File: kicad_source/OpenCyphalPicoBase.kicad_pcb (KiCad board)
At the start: 2 copper layers, 52 x 36 mm, 60 parts, among them CN1 RASPBERRYPI_PICO, CN11 CONN_02X03, CN12 Conn_01x03, CN2 SM04B-SRSS-TB, CN3 SM04B-SRSS-TB, CN4 GH_SM04B-GHS-TB, CN5 GH_SM04B-GHS-TB, CN6 691322310002, CN7 CONN_02X03, CN8 Conn_02x08_Odd_Even, SW1 SPST, U3 24LC64, U8 MCP2515, U9 SN65HVD232, Y1 16MHz

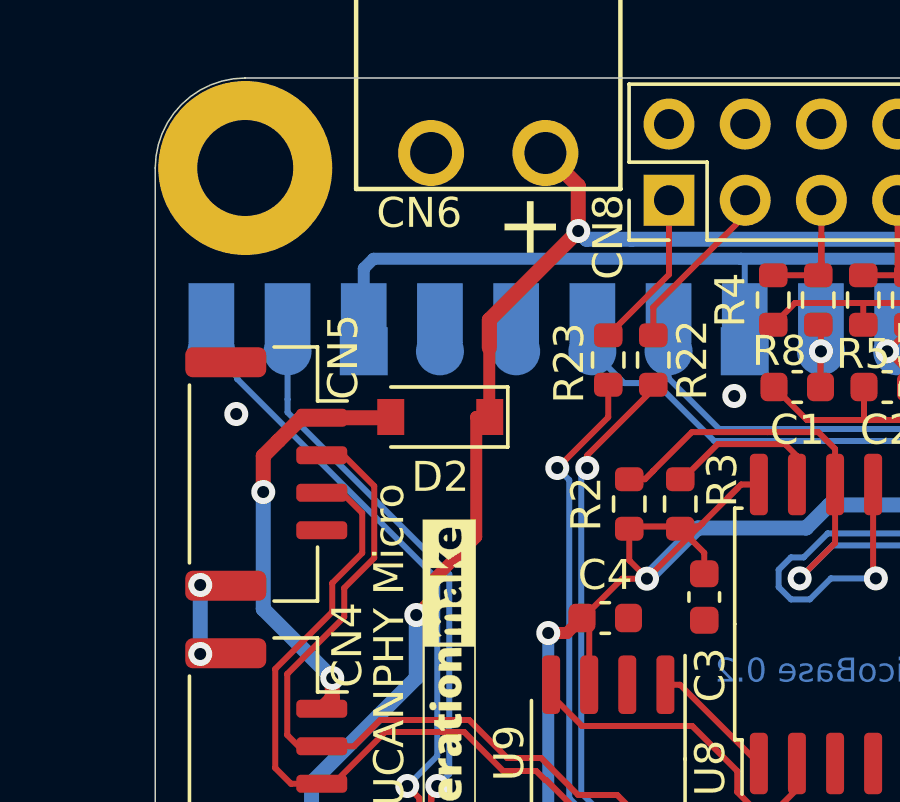
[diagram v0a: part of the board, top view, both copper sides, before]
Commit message: added poly fuse
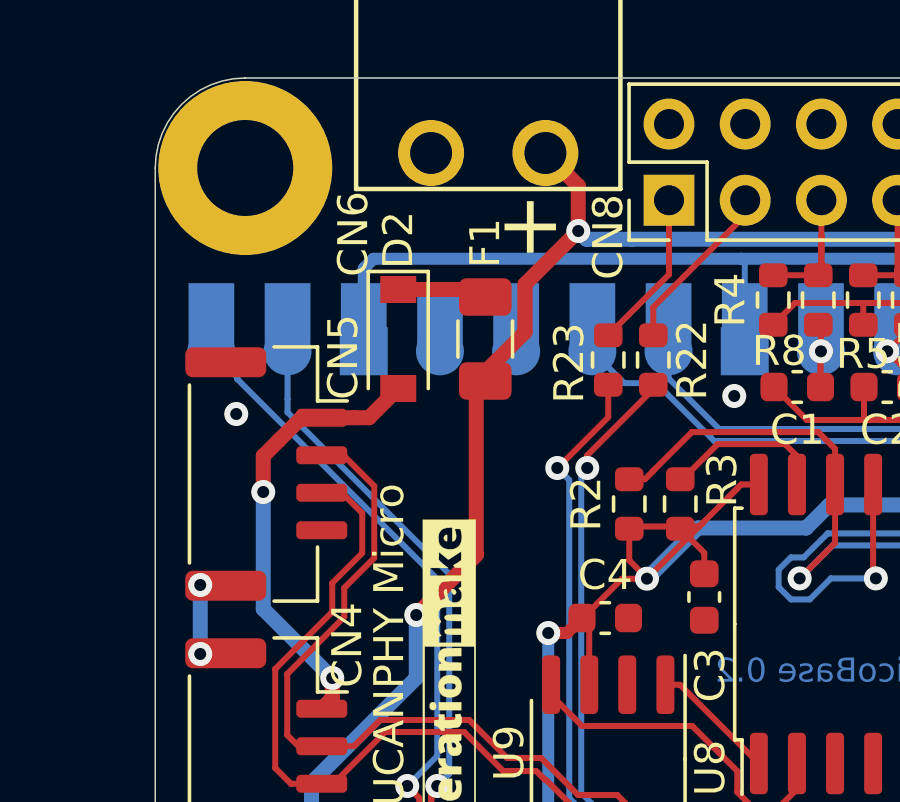
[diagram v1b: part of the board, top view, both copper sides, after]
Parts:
- added F1: nanoSMDC050F, Fuse:Fuse_1206_3216Metric, F.Cu at (75.0, 82.7)
- moved D2 2.95 mm to (72.1, 82.7), turned to -90 degrees
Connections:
- D2 pad 1: +BATT -> Net-(D2-Pad1)
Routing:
- net Net-(D2-Pad1): track 0.00 -> 4.26 mm
- net /MCP2515/CANVCC: track 14.3 -> 15.0 mm
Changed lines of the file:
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@@
   (net 65 "unconnected-(MECH4-Pad1)")
   (net 66 "unconnected-(U9-Pad5)")
+  (net 67 "Net-(D2-Pad1)")
   (footprint "MECH_mounting_holes:MHP_3.2_5.8" (layer "F.Cu")
     (at 67 77)
@@
   )
   (footprint "Diode_SMD:D_SOD-123" (layer "F.Cu")
-    (at 73.5 85.3 180)
+    (at 72.1 82.7 -90)
     (descr "SOD-123")
     (tags "SOD-123")
@@
     (property "Sheetname" "MCP2515")
     (attr smd)
-    (fp_text reference "D2" (at 0 -2 180) (layer "F.SilkS")
+    (fp_text reference "D2" (at -3.3 0 90) (layer "F.SilkS")
       (effects (font (size 1 1) (thickness 0.15)))
     )
-    (fp_text value "MBR0530T1G" (at 0 2.1 180) (layer "F.Fab")
+    (fp_text value "MBR0530T1G" (at 0 2.1 90) (layer "F.Fab")
       (effects (font (size 1 1) (thickness 0.15)))
     )
-    (fp_text user "${REFERENCE}" (at 0 -2 180) (layer "F.Fab")
+    (fp_text user "${REFERENCE}" (at 0 -2 90) (layer "F.Fab")
       (effects (font (size 1 1) (thickness 0.15)))
     )
@@
     (fp_line (start 1.4 0.9) (end -1.4 0.9) (layer "F.Fab") (width 0.1))
     (fp_line (start -1.4 0.9) (end -1.4 -0.9) (layer "F.Fab") (width 0.1))
-    (pad "1" smd rect (at -1.65 0 180) (size 0.9 1.2) (layers "F.Cu" "F.Paste" "F.Mask")
-      (net 15 "+BATT") (pinfunction "K") (pintype "passive"))
-    (pad "2" smd rect (at 1.65 0 180) (size 0.9 1.2) (layers "F.Cu" "F.Paste" "F.Mask")
+    (pad "1" smd rect (at -1.65 0 270) (size 0.9 1.2) (layers "F.Cu" "F.Paste" "F.Mask")
+      (net 67 "Net-(D2-Pad1)") (pinfunction "K") (pintype "passive"))
+    (pad "2" smd rect (at 1.65 0 270) (size 0.9 1.2) (layers "F.Cu" "F.Paste" "F.Mask")
       (net 11 "/MCP2515/CANVCC") (pinfunction "A") (pintype "passive"))
     (model "${KICAD6_3DMODEL_DIR}/Diode_SMD.3dshapes/D_SOD-123.wrl"
@@
     (property "Sheetname" "")
     (attr through_hole)
-    (fp_text reference "CN6" (at 2.3 -2) (layer "F.SilkS")
+    (fp_text reference "CN6" (at 4.5 -2.7 90) (layer "F.SilkS")
       (effects (font (size 1 1) (thickness 0.15)))
     )
@@
     )
   )
+  (footprint "Fuse:Fuse_1206_3216Metric" (layer "F.Cu")
+    (at 75 82.7 90)
+    (descr "Fuse SMD 1206 (3216 Metric), square (rectangular) end terminal, IPC_7351 nominal, (Body size source: http://www.tortai-tech.com/upload/download/2011102023233369053.pdf), generated with kicad-footprint-generator")
+    (tags "fuse")
+    (property "Sheetfile" "Datei: mcp2515.kicad_sch")
+    (property "Sheetname" "MCP2515")
+    (attr smd)
+    (fp_text reference "F1" (at 3.2 0 90) (layer "F.SilkS")
+      (effects (font (size 1 1) (thickness 0.15)))
+    )
+    (fp_text value "nanoSMDC050F" (at 0 1.82 90) (layer "F.Fab")
+      (effects (font (size 1 1) (thickness 0.15)))
+    )
+    (fp_text user "${REFERENCE}" (at 0 0 90) (layer "F.Fab")
+      (effects (font (size 0.8 0.8) (thickness 0.12)))
+    )
+    (fp_line (start -0.602064 0.91) (end 0.602064 0.91) (layer "F.SilkS") (width 0.12))
+    (fp_line (start -0.602064 -0.91) (end 0.602064 -0.91) (layer "F.SilkS") (width 0.12))
+    (fp_line (start 2.28 -1.12) (end 2.28 1.12) (layer "F.CrtYd") (width 0.05))
+    (fp_line (start -2.28 -1.12) (end 2.28 -1.12) (layer "F.CrtYd") (width 0.05))
+    (fp_line (start 2.28 1.12) (end -2.28 1.12) (layer "F.CrtYd") (width 0.05))
+    (fp_line (start -2.28 1.12) (end -2.28 -1.12) (layer "F.CrtYd") (width 0.05))
+    (fp_line (start -1.6 0.8) (end -1.6 -0.8) (layer "F.Fab") (width 0.1))
+    (fp_line (start 1.6 0.8) (end -1.6 0.8) (layer "F.Fab") (width 0.1))
+    (fp_line (start -1.6 -0.8) (end 1.6 -0.8) (layer "F.Fab") (width 0.1))
+    (fp_line (start 1.6 -0.8) (end 1.6 0.8) (layer "F.Fab") (width 0.1))
+    (pad "1" smd roundrect (at -1.4 0 90) (size 1.25 1.75) (layers "F.Cu" "F.Paste" "F.Mask") (roundrect_rratio 0.2)
+      (net 15 "+BATT") (pintype "passive"))
+    (pad "2" smd roundrect (at 1.4 0 90) (size 1.25 1.75) (layers "F.Cu" "F.Paste" "F.Mask") (roundrect_rratio 0.2)
+      (net 67 "Net-(D2-Pad1)") (pintype "passive"))
+    (model "${KICAD6_3DMODEL_DIR}/Fuse.3dshapes/Fuse_1206_3216Metric.wrl"
+      (offset (xyz 0 0 0))
+      (scale (xyz 1 1 1))
+      (rotate (xyz 0 0 0))
+    )
+  )
   (footprint "labels:generationmake_small_solder" (layer "B.Cu")
     (at 89.61905 110.93645 180)
@@
   (segment (start 69.55 85.325) (end 68.875 85.325) (width 0.5) (layer "F.Cu") (net 11))
   (segment (start 68.1 86.1) (end 67.6 86.6) (width 0.5) (layer "F.Cu") (net 11))
-  (segment (start 69.55 85.325) (end 71.84 85.325) (width 0.5) (layer "F.Cu") (net 11))
+  (segment (start 71.125 85.325) (end 72.1 84.35) (width 0.5) (layer "F.Cu") (net 11))
+  (segment (start 69.55 85.325) (end 70.625 85.325) (width 0.5) (layer "F.Cu") (net 11))
   (segment (start 68.875 85.325) (end 68.1 86.1) (width 0.5) (layer "F.Cu") (net 11))
   (segment (start 67.6 86.6) (end 67.6 87.8) (width 0.5) (layer "F.Cu") (net 11))
-  (segment (start 71.84 85.325) (end 71.865 85.3) (width 0.5) (layer "F.Cu") (net 11))
+  (segment (start 70.625 85.325) (end 71.125 85.325) (width 0.5) (layer "F.Cu") (net 11))
   (via (at 69.9 94) (size 0.8) (drill 0.4) (layers "F.Cu" "B.Cu") (net 11))
   (via (at 67.6 87.8) (size 0.8) (drill 0.4) (layers "F.Cu" "B.Cu") (net 11))
@@
   (segment (start 106.9 103.425) (end 106.7 103.225) (width 0.2) (layer "F.Cu") (net 14))
   (segment (start 78.1 79.1) (end 78.1 77.595) (width 0.5) (layer "F.Cu") (net 15))
+  (segment (start 74.7 84.1) (end 74.7 89.9) (width 0.5) (layer "F.Cu") (net 15))
   (segment (start 107.6 79.8) (end 108.2 79.2) (width 0.5) (layer "F.Cu") (net 15))
   (segment (start 105.7 85.1) (end 105.7 83.6) (width 0.5) (layer "F.Cu") (net 15))
-  (segment (start 75.135 85.3) (end 75.135 83) (width 0.4) (layer "F.Cu") (net 15))
   (segment (start 106.7 86.1) (end 105.7 85.1) (width 0.5) (layer "F.Cu") (net 15))
-  (segment (start 73.2 91.4) (end 72.7 91.9) (width 0.4) (layer "F.Cu") (net 15))
-  (segment (start 74.7 85.3) (end 75.135 85.3) (width 0.4) (layer "F.Cu") (net 15))
-  (segment (start 75.135 82.065) (end 78.1 79.1) (width 0.5) (layer "F.Cu") (net 15))
+  (segment (start 76.325 80.875) (end 76.325 82.475) (width 0.5) (layer "F.Cu") (net 15))
+  (segment (start 76.325 82.475) (end 74.7 84.1) (width 0.5) (layer "F.Cu") (net 15))
   (segment (start 78.6 103.425) (end 78.6 104.2) (width 0.2) (layer "F.Cu") (net 15))
   (segment (start 108.05 86.1) (end 106.7 86.1) (width 0.5) (layer "F.Cu") (net 15))
+  (segment (start 78.1 79.1) (end 76.325 80.875) (width 0.5) (layer "F.Cu") (net 15))
   (segment (start 105.7 83.6) (end 106.3 83) (width 0.5) (layer "F.Cu") (net 15))
   (segment (start 107.3 83) (end 107.6 82.7) (width 0.5) (layer "F.Cu") (net 15))
   (segment (start 107.6 82.7) (end 107.6 79.8) (width 0.5) (layer "F.Cu") (net 15))
-  (segment (start 74.7 89.3) (end 74.7 85.3) (width 0.4) (layer "F.Cu") (net 15))
-  (segment (start 73.2 90.8) (end 74.7 89.3) (width 0.4) (layer "F.Cu") (net 15))
-  (segment (start 75.135 83) (end 75.135 82.065) (width 0.5) (layer "F.Cu") (net 15))
   (segment (start 78.6 104.2) (end 78.9 104.5) (width 0.2) (layer "F.Cu") (net 15))
   (segment (start 78.1 77.595) (end 77.005 76.5) (width 0.5) (layer "F.Cu") (net 15))
-  (segment (start 73.2 90.8) (end 73.2 91.4) (width 0.4) (layer "F.Cu") (net 15))
   (segment (start 106.3 83) (end 107.3 83) (width 0.5) (layer "F.Cu") (net 15))
+  (segment (start 74.7 89.9) (end 72.7 91.9) (width 0.5) (layer "F.Cu") (net 15))
   (via (at 72.7 91.9) (size 0.8) (drill 0.4) (layers "F.Cu" "B.Cu") (net 15))
   (via (at 78.9 104.5) (size 0.8) (drill 0.4) (layers "F.Cu" "B.Cu") (net 15))
@@
   (segment (start 76.03 81.84) (end 76.03 83.11) (width 0.4) (layer "B.Cu") (net 60))
   (segment (start 73.49 81.84) (end 73.49 83.11) (width 0.4) (layer "B.Cu") (net 61))
+  (segment (start 73.55 81.05) (end 74.45 81.05) (width 0.5) (layer "F.Cu") (net 67))
+  (segment (start 73.55 81.05) (end 74.75 81.05) (width 0.5) (layer "F.Cu") (net 67))
+  (segment (start 73.55 81.05) (end 72.1 81.05) (width 0.5) (layer "F.Cu") (net 67))
+  (segment (start 74.45 81.05) (end 74.7 81.3) (width 0.5) (layer "F.Cu") (net 67))
+  (segment (start 74.75 81.05) (end 75 81.3) (width 0.5) (layer "F.Cu") (net 67))
   (zone (net 2) (net_name "GND") (layer "F.Cu") (hatch edge 0.508)
     (connect_pads (clearance 0.508))

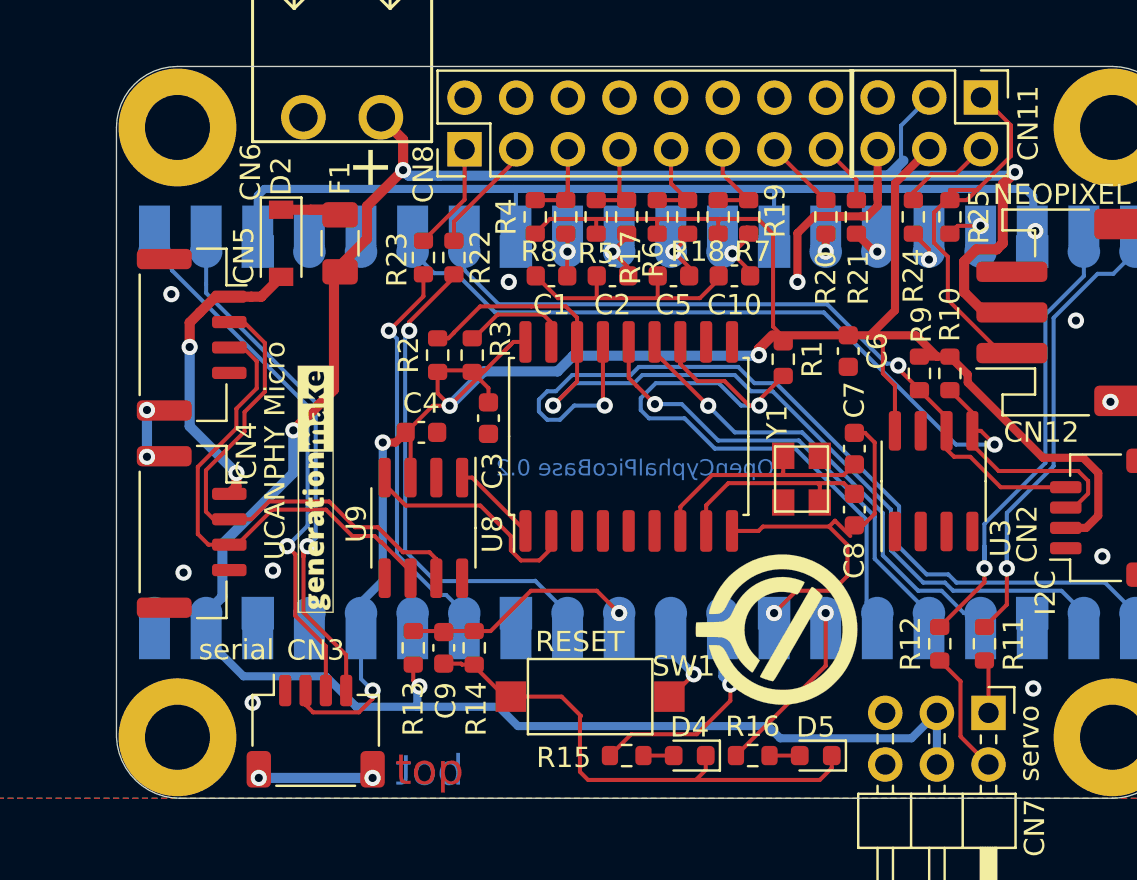
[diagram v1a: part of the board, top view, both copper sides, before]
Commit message: added capacitor on +BATT
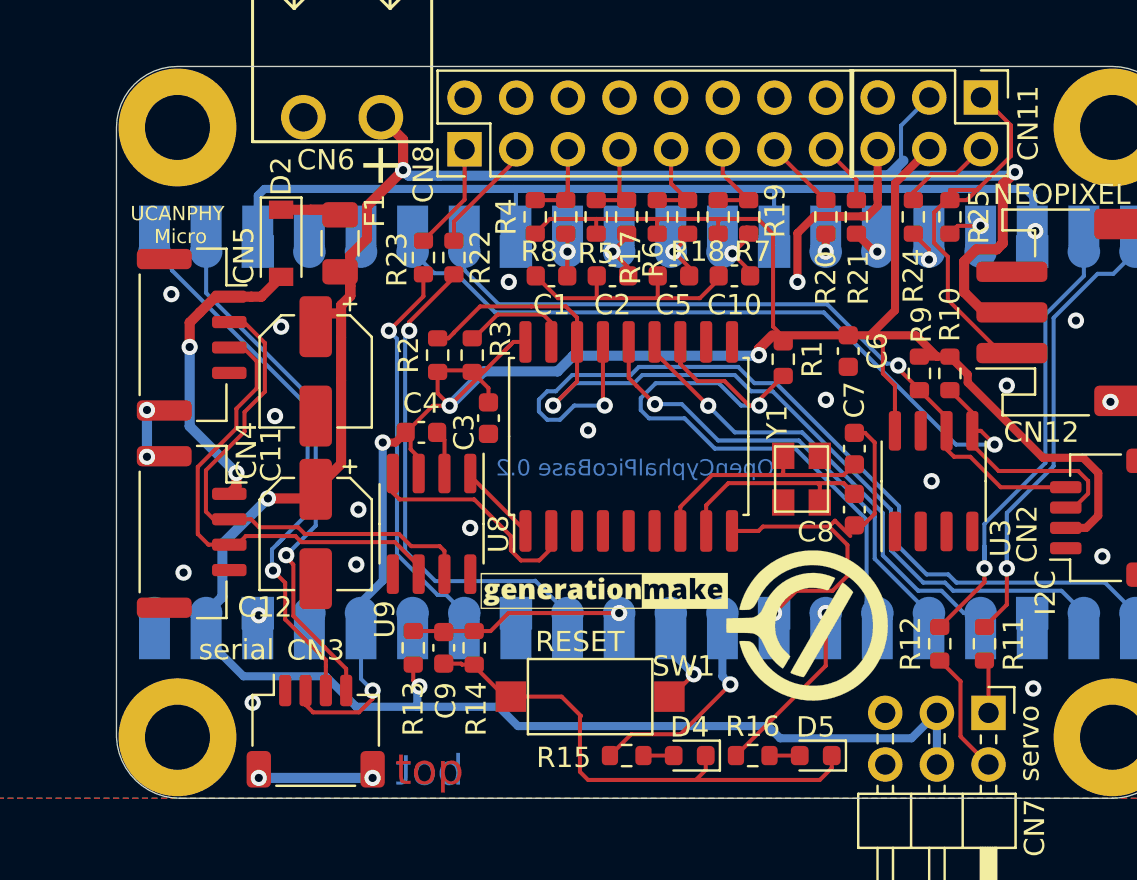
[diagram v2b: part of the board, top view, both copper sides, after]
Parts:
- added C11: 100 uF / 6,3 V, Capacitor_SMD:CP_Elec_5x5.3, F.Cu at (73.8, 89.0)
- added C12: 100 uF / 6,3 V, Capacitor_SMD:CP_Elec_5x5.3, F.Cu at (73.8, 97.0)
- moved L1 13.8 mm to (88.0, 102.4), turned to 0 degrees
- moved L3 1.51 mm to (98.0, 101.5)
- moved U9 0.45 mm to (79.5, 96.5)
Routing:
- net +BATT: track 119.7 -> 123.7 mm
- net GND: track 115.9 -> 118.0 mm, vias 11 -> 20
- net /SER_TX: track 27.2 -> 28.2 mm
- net /+BATT_MEAS: track 12.7 -> 11.8 mm
- net /MCP2515/CANL: track 24.3 -> 23.8 mm
